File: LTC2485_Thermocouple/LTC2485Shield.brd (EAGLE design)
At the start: 53 x 26.7 mm, 13 parts

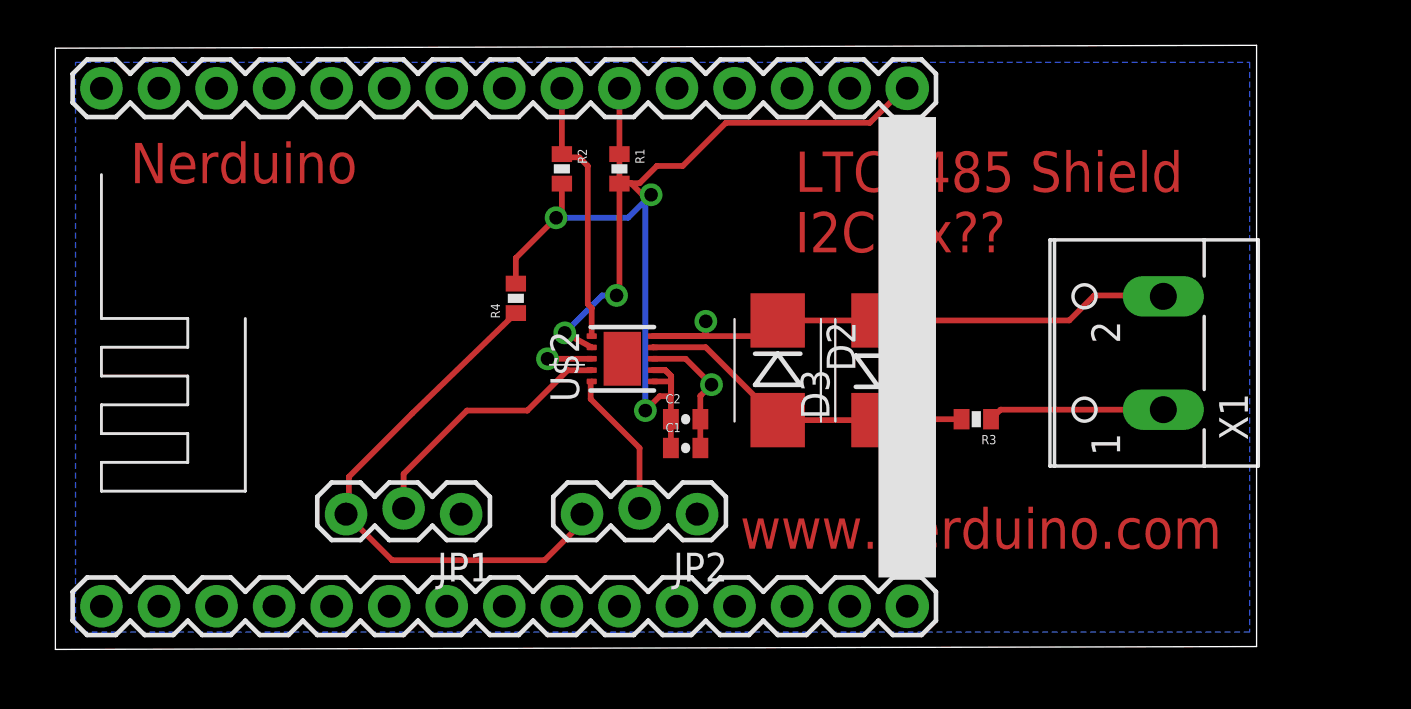
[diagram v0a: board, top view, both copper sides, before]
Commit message: Updated stencil text Added PCA9685 and ITG3200 shields
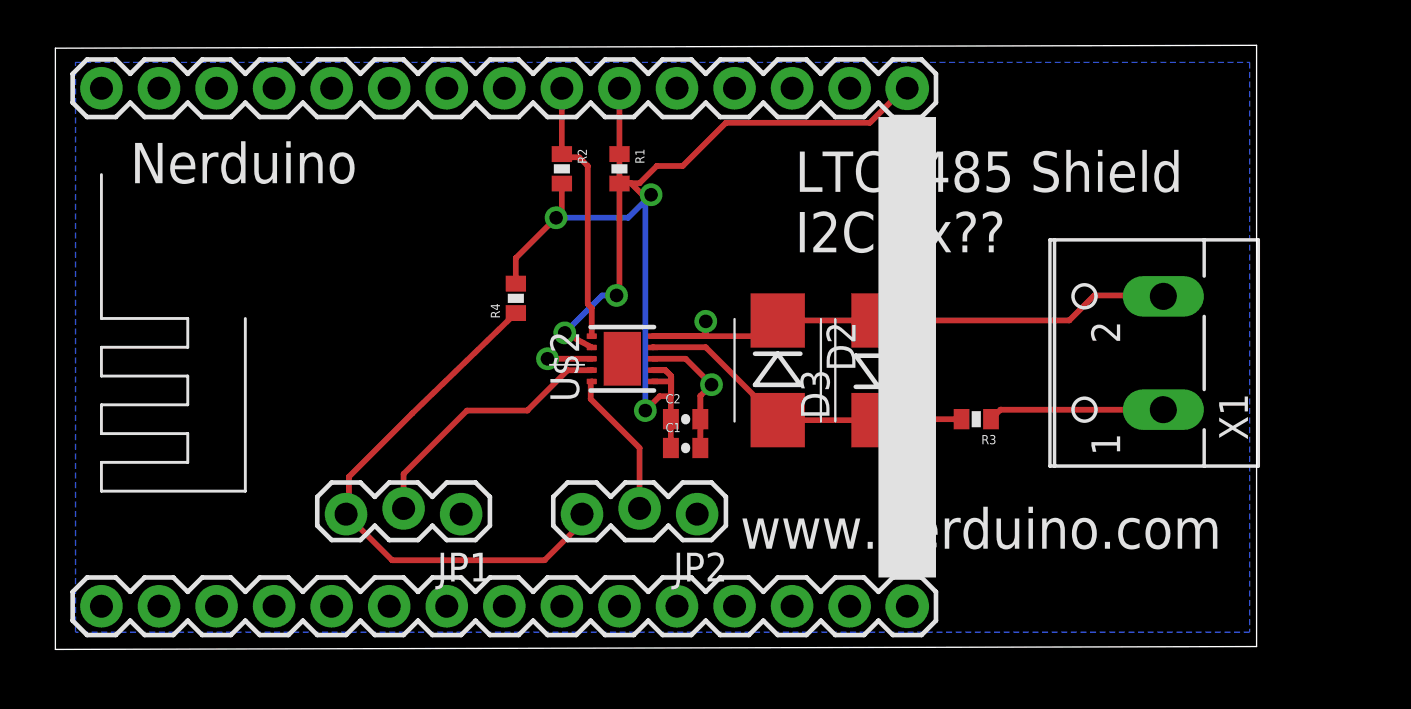
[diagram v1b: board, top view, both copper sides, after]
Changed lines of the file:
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@@
 <wire x1="53.518" y1="27.295" x2="0.508" y2="27.168" width="0" layer="20"/>
 <wire x1="0.508" y1="27.168" x2="0.508" y2="0.635" width="0" layer="20"/>
-<text x="3.81" y="21.209" size="1.778" layer="1">Nerduino</text>
-<text x="33.147" y="20.828" size="1.778" layer="1">LTC2485 Shield</text>
-<text x="33.147" y="18.161" size="1.778" layer="1">I2C 0x??</text>
-<text x="30.734" y="5.08" size="1.778" layer="1">www.nerduino.com</text>
+<text x="3.81" y="21.209" size="1.778" layer="121">Nerduino</text>
+<text x="33.147" y="20.828" size="1.778" layer="121">LTC2485 Shield</text>
+<text x="33.147" y="18.161" size="1.778" layer="121">I2C 0x??</text>
+<text x="30.734" y="5.08" size="1.778" layer="121">www.nerduino.com</text>
 </plain>
 <attributes>

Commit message: Added OLED Shield Added LiPo Battery Charger Shield Updated outlines of all shields to match the cutout of the nodemcu board
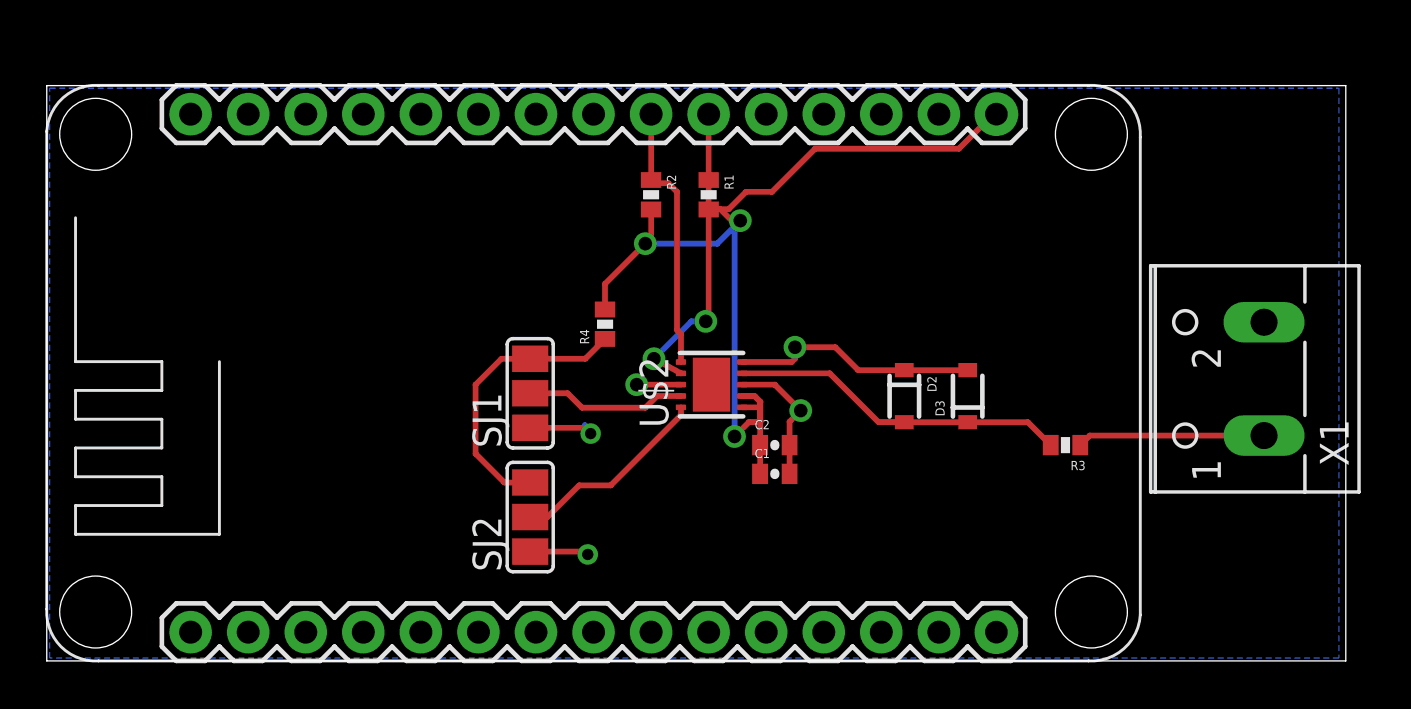
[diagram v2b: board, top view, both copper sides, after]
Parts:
- removed JP1, JP2: (no value), SparkFun:1X03_LOCK
- added SJ1, SJ2: (no value), SparkFun:SJ_2
- D2, D3: device SparkFun:SMB-DIODE -> SparkFun:SOD-323
- moved D2 5.70 mm to (38.0, 11.8)
- moved X1 4.59 mm to (52.6, 12.6)
- moved D3 4.10 mm to (40.8, 11.8)
- moved C1 4.10 mm to (32.3, 8.38)
- moved C2 4.10 mm to (32.3, 9.65)
- moved R1 4.10 mm to (29.3, 20.7)
- moved R2 4.10 mm to (26.8, 20.7)
- moved R4 4.10 mm to (24.8, 15.0)
- moved U$1 4.10 mm to (24.3, 6.48)
- moved R3 4.10 mm to (45.1, 9.65)
- moved U$2 4.10 mm to (29.5, 12.3)
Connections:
- net GND: now also D2.1, D3.2, SJ1.1, SJ2.1, U$1.10, U$1.17, U$1.24; no longer D2.C, D3.A, JP1.1, JP2.1
- net N$3: now also D2.2, D3.1; no longer D2.A, D3.C
- net N$6: now also SJ1.3, SJ2.3; no longer JP1.3, JP2.3
- net N$7: now also SJ1.2; no longer JP1.2
- net N$9: now also SJ2.2; no longer JP2.2
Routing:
- net N$6: track 24.3 -> 12.5 mm
- net GND: track 35.1 -> 25.9 mm, vias 3 -> 5
- net N$7: track 11.7 -> 7.13 mm
- net N$9: track 6.52 -> 8.86 mm
- net N$1: track 7.78 -> 8.29 mm
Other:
- board size 53 x 26.7 mm -> 57.3 x 25.4 mm
- board text added: "NERDUINO LTC2485 Shield I2C 0x?? www.nerduino.com"
- board text removed: "I2C 0x??"
- board text removed: "LTC2485 Shield"
- board text removed: "Nerduino"
- board text removed: "www.nerduino.com"

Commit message: Updated the i2c pins to all shields to use d11/d12  as these pins will have dual use with the upcoming wifimcu Added FM24W256  Fram shield Added X95840 Digital potentiometer Shield Added AD5696 DAC Shield
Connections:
- net GND: no longer U$1.24
- net N$2: now also U$1.5; no longer U$1.21
- net N$8: now also U$1.4; no longer U$1.22
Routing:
- net N$8: track 11.8 -> 37.0 mm
- net N$2: track 13.5 -> 28.2 mm
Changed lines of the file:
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@@
 <contactref element="U$1" pad="10"/>
 <contactref element="U$1" pad="17"/>
-<contactref element="U$1" pad="24"/>
 <contactref element="SJ1" pad="1"/>
 <contactref element="SJ2" pad="1"/>
@@
 </signal>
 <signal name="N$2">
-<contactref element="U$1" pad="21"/>
 <contactref element="U$2" pad="7"/>
 <contactref element="R1" pad="1"/>
-<wire x1="29.337" y1="24.257" x2="29.337" y2="21.351" width="0.254" layer="1"/>
 <wire x1="29.337" y1="21.351" x2="29.337" y2="15.24" width="0.254" layer="1"/>
 <wire x1="29.337" y1="15.24" x2="29.21" y2="15.113" width="0.254" layer="1"/>
@@
 <wire x1="28.575" y1="15.113" x2="26.924" y2="13.462" width="0.254" layer="16"/>
 <via x="26.924" y="13.462" extent="1-16" drill="0.6"/>
-<wire x1="26.924" y1="13.462" x2="28.106" y2="12.827" width="0.254" layer="1"/>
 <wire x1="28.106" y1="12.827" x2="28.114" y2="12.819" width="0.254" layer="1"/>
+<contactref element="U$1" pad="5"/>
+<wire x1="16.637" y1="1.397" x2="16.637" y2="5.207" width="0.254" layer="16"/>
+<wire x1="16.637" y1="5.207" x2="24.892" y2="13.462" width="0.254" layer="16"/>
+<wire x1="24.892" y1="13.462" x2="26.924" y2="13.462" width="0.254" layer="16"/>
+<wire x1="28.106" y1="12.827" x2="27.559" y2="12.827" width="0.254" layer="1"/>
+<wire x1="27.559" y1="12.827" x2="26.924" y2="13.462" width="0.254" layer="1"/>
 </signal>
 <signal name="N$8">
 <contactref element="U$2" pad="6"/>
-<contactref element="U$1" pad="22"/>
 <contactref element="R2" pad="1"/>
 <wire x1="28.114" y1="13.319" x2="28.114" y2="14.558" width="0.254" layer="1"/>
@@
 <wire x1="27.559" y1="21.209" x2="26.939" y2="21.209" width="0.254" layer="1"/>
 <wire x1="26.939" y1="21.209" x2="26.797" y2="21.351" width="0.254" layer="1"/>
-<wire x1="26.797" y1="21.351" x2="26.797" y2="24.257" width="0.254" layer="1"/>
+<contactref element="U$1" pad="4"/>
+<wire x1="14.097" y1="1.397" x2="14.097" y2="13.462" width="0.254" layer="1"/>
+<wire x1="14.097" y1="13.462" x2="21.971" y2="21.336" width="0.254" layer="1"/>
+<wire x1="21.971" y1="21.336" x2="26.782" y2="21.336" width="0.254" layer="1"/>
+<wire x1="26.782" y1="21.336" x2="26.797" y2="21.351" width="0.254" layer="1"/>
 </signal>
 <signal name="N$1">
